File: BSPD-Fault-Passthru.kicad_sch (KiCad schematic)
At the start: 12 parts, among them Q12 SI2347DS-T1-GE3, Q13 SI2318CDS-T1-GE3

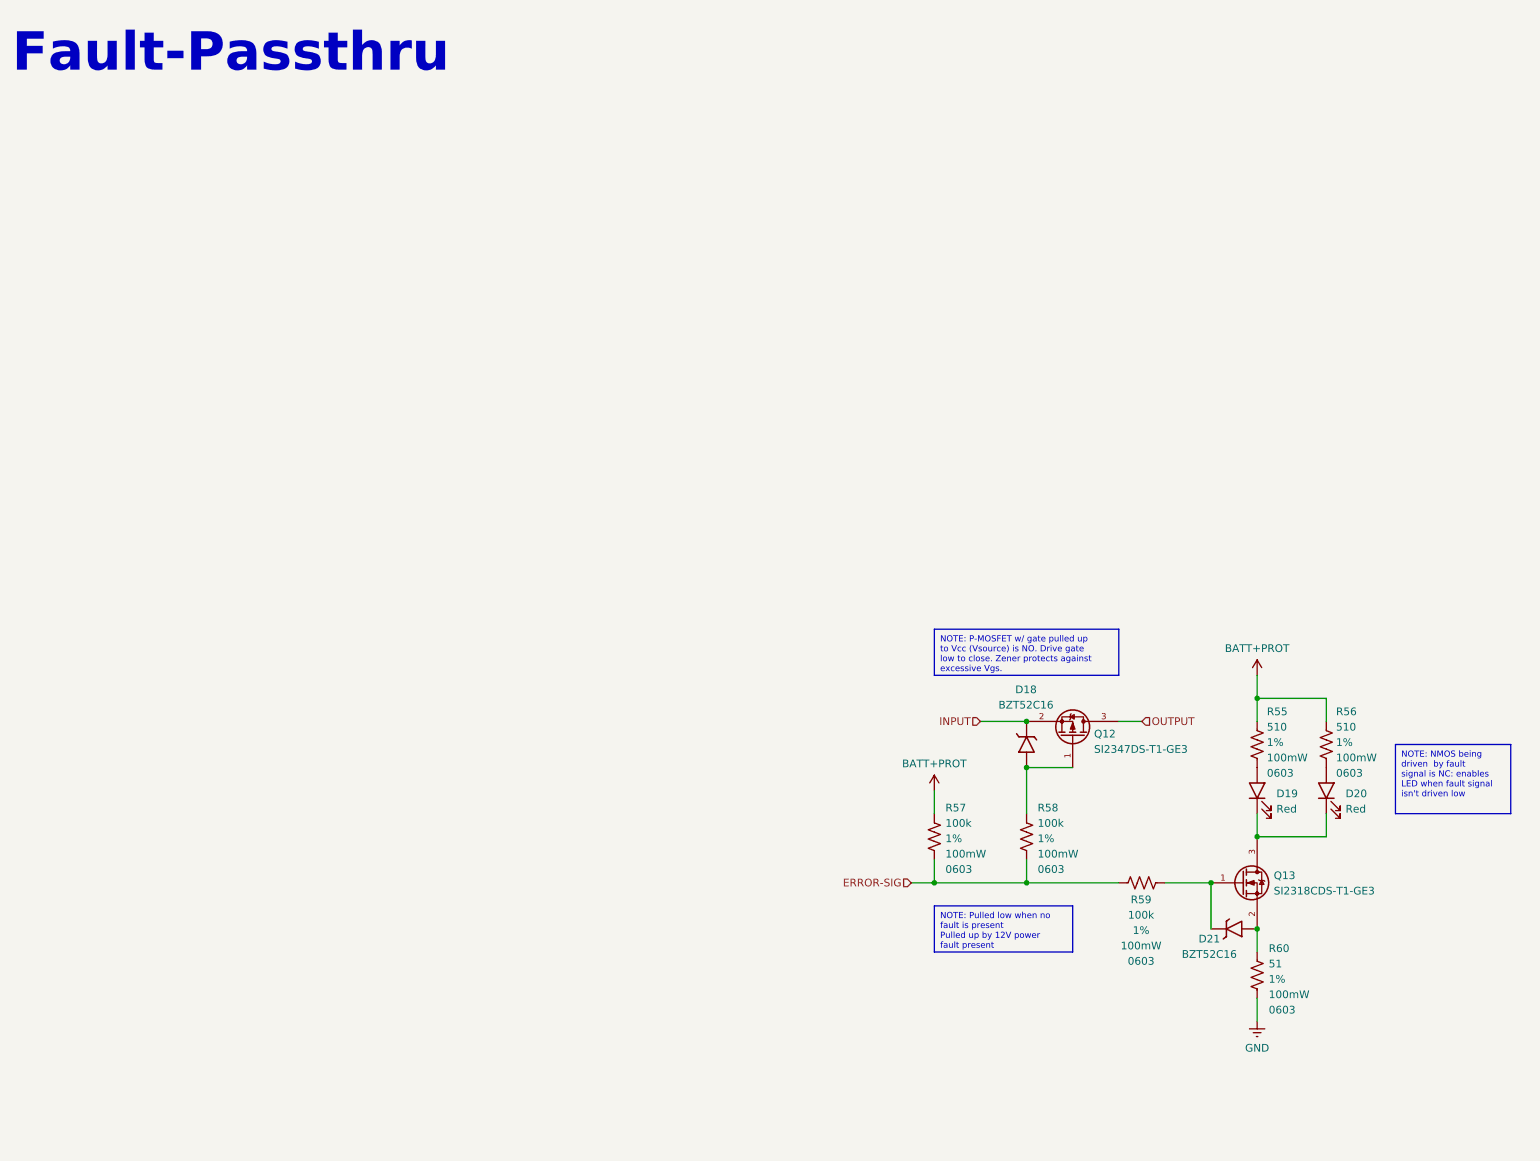
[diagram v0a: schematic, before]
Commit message: changed BSPD, BMS fault logic to match Mk11 specs, all signals going back to VCU have 12V fault, 0V no fault readings, connector symbols/footprints left for next push
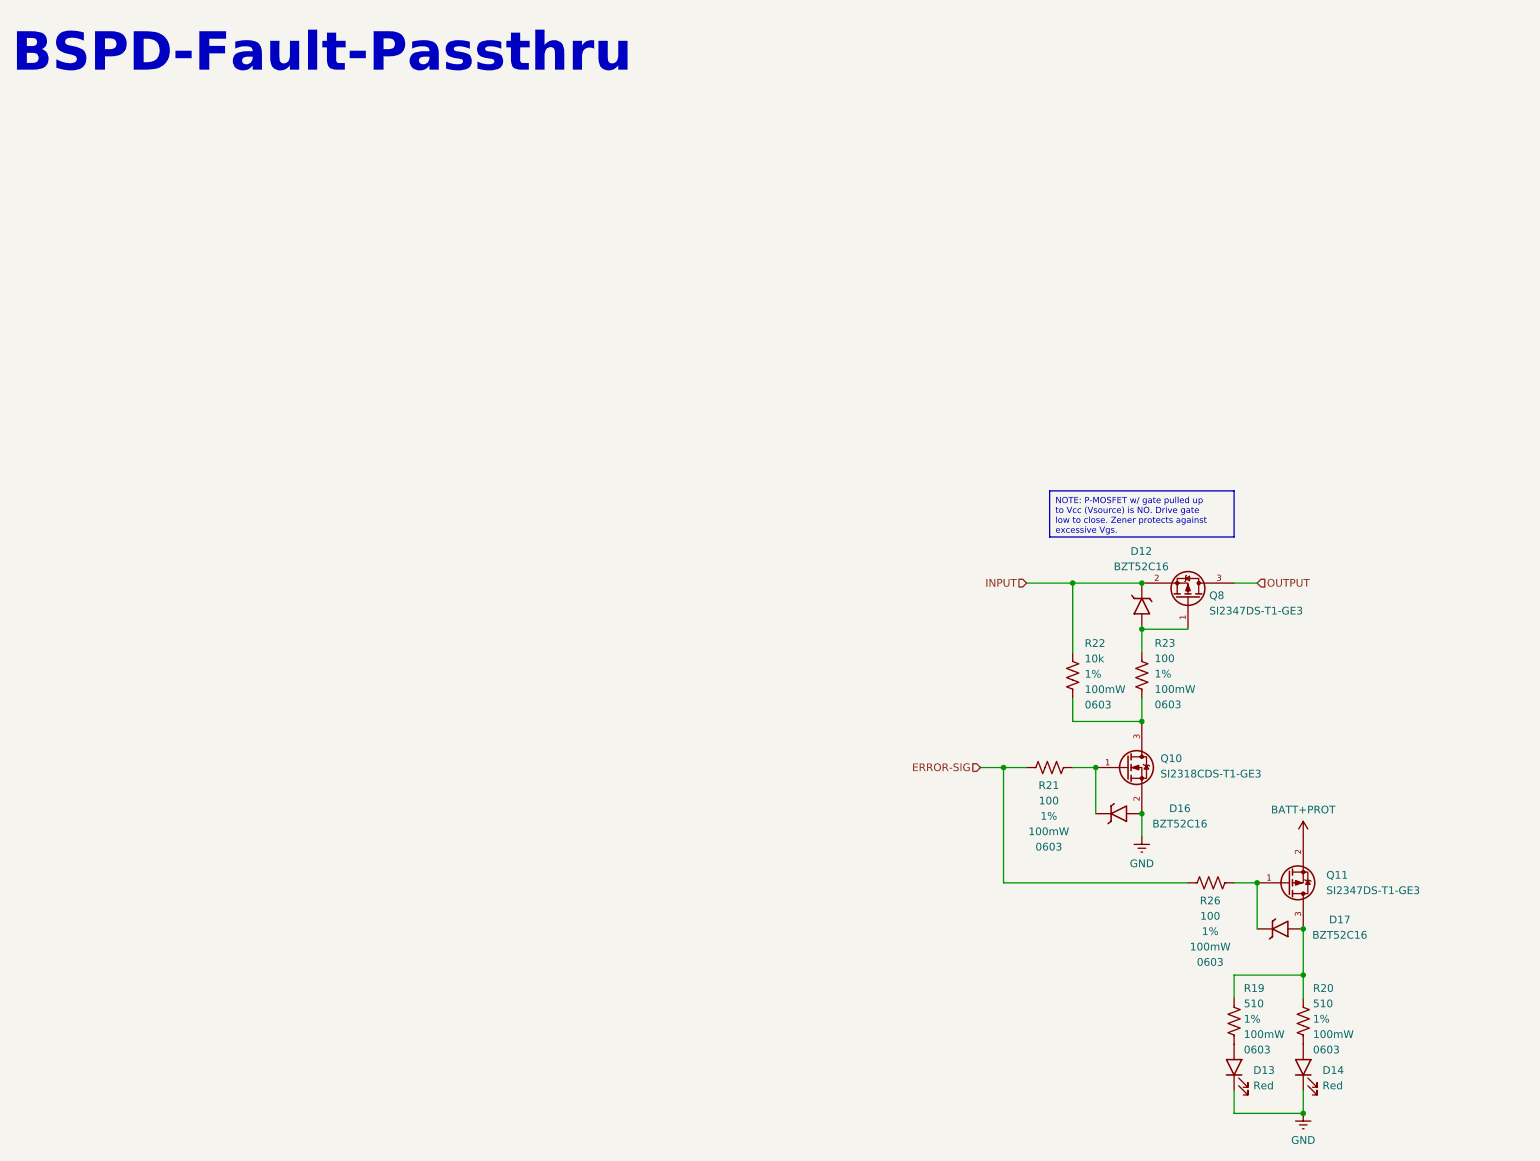
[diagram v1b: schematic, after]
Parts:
- removed D18, D21: BZT52C16, Diode_SMD:D_SOD-123, symbol -Diodes-Zener:BZT52C16
- removed D19, D20: Red, LED_SMD:LED_0805_2012Metric, symbol -Diodes-LED:NCD0805R1
- removed Q12: SI2347DS-T1-GE3, Package_TO_SOT_SMD:SOT-23-3, symbol -MOSFET-P-Channel:SI2347DS-T1-GE3
- removed Q13: SI2318CDS-T1-GE3, Package_TO_SOT_SMD:SOT-23-3, symbol -MOSFET-N-Channel:SI2318CDS-T1-GE3
- removed R55, R56: 510, Resistor_SMD:R_0603_1608Metric_Pad0.98x0.95mm_HandSolder, symbol -R-SMD-0603:R-0603-510-1%-100mW-100PPM
- removed R57, R58, R59: 100k, Resistor_SMD:R_0603_1608Metric_Pad0.98x0.95mm_HandSolder, symbol -R-SMD-0603:R-0603-100k-1%-100mW-100PPM
- removed R60: 51, Resistor_SMD:R_0603_1608Metric_Pad0.98x0.95mm_HandSolder, symbol -R-SMD-0603:R-0603-51-1%-100mW-100PPM
- added D12, D16, D17: BZT52C16, Diode_SMD:D_SOD-123, symbol -Diodes-Zener:BZT52C16
- added D13, D14: Red, LED_SMD:LED_0805_2012Metric, symbol -Diodes-LED:NCD0805R1
- added Q10: SI2318CDS-T1-GE3, Package_TO_SOT_SMD:SOT-23-3, symbol -MOSFET-N-Channel:SI2318CDS-T1-GE3
- added Q11, Q8: SI2347DS-T1-GE3, Package_TO_SOT_SMD:SOT-23-3, symbol -MOSFET-P-Channel:SI2347DS-T1-GE3
- added R19, R20: 510, Resistor_SMD:R_0603_1608Metric_Pad0.98x0.95mm_HandSolder, symbol -R-SMD-0603:R-0603-510-1%-100mW-100PPM
- added R21, R23, R26: 100, Resistor_SMD:R_0603_1608Metric_Pad0.98x0.95mm_HandSolder, symbol -R-SMD-0603:R-0603-100-1%-100mW-100PPM
- added R22: 10k, Resistor_SMD:R_0603_1608Metric_Pad0.98x0.95mm_HandSolder, symbol -R-SMD-0603:R-0603-10k-1%-100mW-100PPM
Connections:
- net BATT+PROT: now also Q11.2 (S)
- net ERROR-SIG: now also R21.1, R26.1
- net GND: now also D13.1 (K), D14.1 (K), D16.2 (A), Q10.2 (S)
- net INPUT: now also D12.1 (K), Q8.2 (S), R22.2
- net OUTPUT: now also Q8.3 (D)
- new net: D13.2 (A), R19.1
- new net: D14.2 (A), R20.1
- new net: D17.1 (K), Q11.1 (G), R26.2
- new net: D17.2 (A), Q11.3 (D), R19.2, R20.2
- new net: D16.1 (K), Q10.1 (G), R21.2
- new net: Q10.3 (D), R22.1, R23.1
- new net: D12.2 (A), Q8.1 (G), R23.2
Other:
- note added: "BSPD-Fault-Passthru"
- note removed: "Fault-Passthru"
